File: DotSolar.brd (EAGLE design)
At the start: 25 x 35 mm, 24 parts, among them IC1 CAT24M010TS, IC2 SI1145, Q1 BSH203, U1 ISL29125

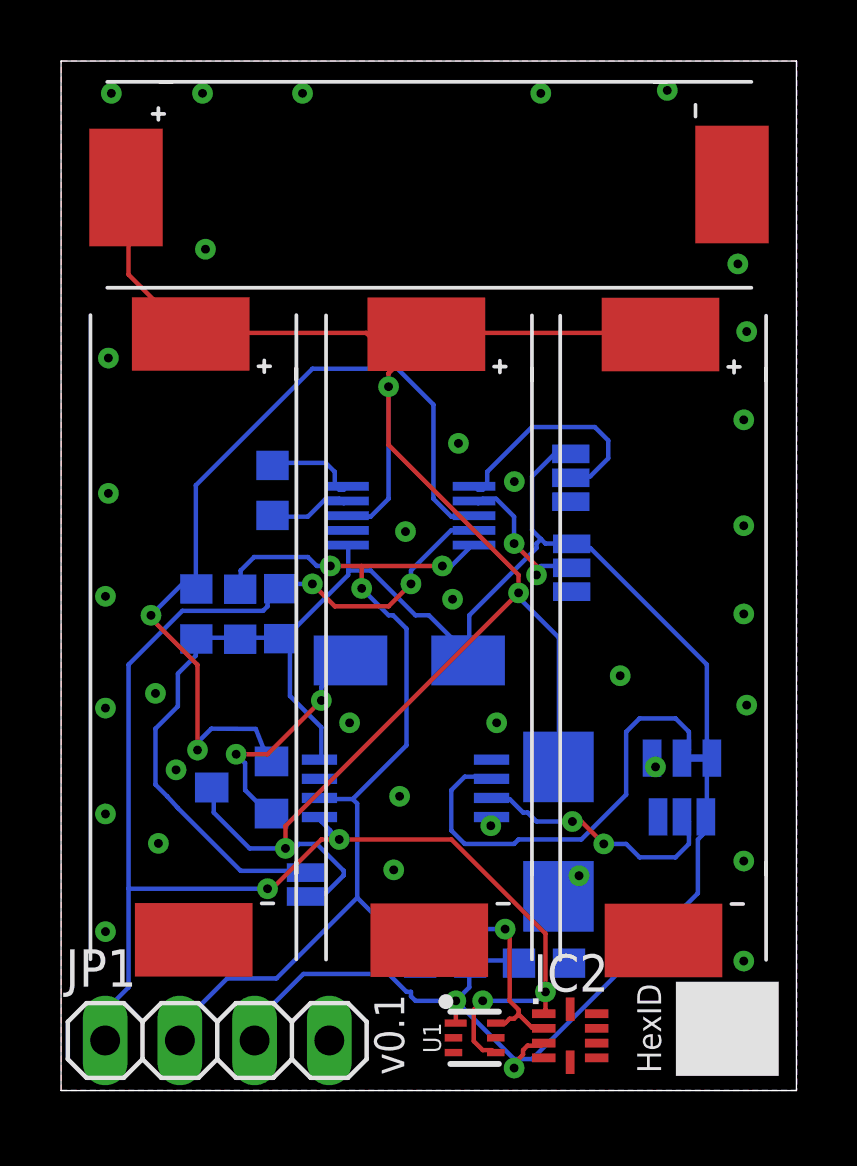
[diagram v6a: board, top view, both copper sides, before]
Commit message: Move zener
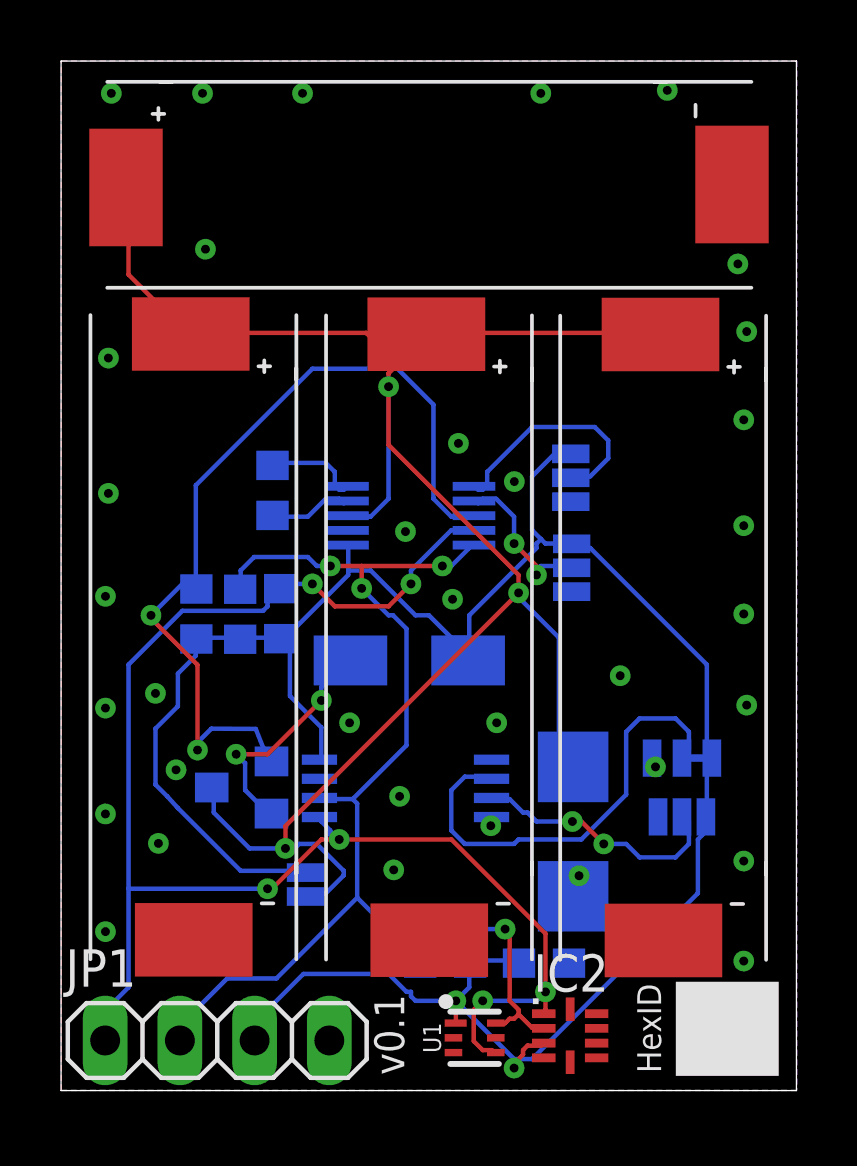
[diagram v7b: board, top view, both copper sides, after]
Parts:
- moved D3 0.50 mm to (17.4, 8.80)
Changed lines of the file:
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@@
 <layer number="22" name="bPlace" color="7" fill="1" visible="yes" active="yes"/>
 <layer number="23" name="tOrigins" color="15" fill="1" visible="no" active="yes"/>
-<layer number="24" name="bOrigins" color="15" fill="1" visible="no" active="yes"/>
+<layer number="24" name="bOrigins" color="15" fill="1" visible="yes" active="yes"/>
 <layer number="25" name="tNames" color="7" fill="1" visible="no" active="yes"/>
 <layer number="26" name="bNames" color="7" fill="1" visible="no" active="yes"/>
@@
 <element name="R2" library="rcl" package="R0603" value="4.7kΩ" x="7.44" y="16.21" rot="MR270"/>
 <element name="R3" library="rcl" package="R0603" value="4.7kΩ" x="6.08" y="16.19" rot="MR270"/>
-<element name="D3" library="diode" package="SMB" value="" x="16.9" y="8.8" rot="MR270"/>
+<element name="D3" library="diode" package="SMB" value="" x="17.4" y="8.8" rot="MR270"/>
 <element name="Q1" library="BSH203" package="SOT-23" value="BSH203" x="6.13" y="10.3" rot="MR270"/>
 <element name="U1" library="SparkFun-Sensors" package="ODFN-6" value="ISL29125" x="14.05" y="1.79">
@@
 <wire x1="11.1252" y1="21.9456" x2="15.5448" y2="17.526" width="0.1524" layer="1"/>
 <wire x1="11.1252" y1="23.9268" x2="11.1252" y2="21.9456" width="0.1524" layer="1"/>
-<wire x1="16.9164" y1="11.1252" x2="16.9" y2="11" width="0.1524" layer="16"/>
+<wire x1="16.9164" y1="11.1252" x2="17.4" y2="11" width="0.1524" layer="16"/>
 <wire x1="7.62" y1="8.9916" x2="7.62" y2="8.2296" width="0.1524" layer="1"/>
 <wire x1="15.5448" y1="16.9164" x2="7.62" y2="8.9916" width="0.1524" layer="1"/>

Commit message: Update tracks for production at Aisler
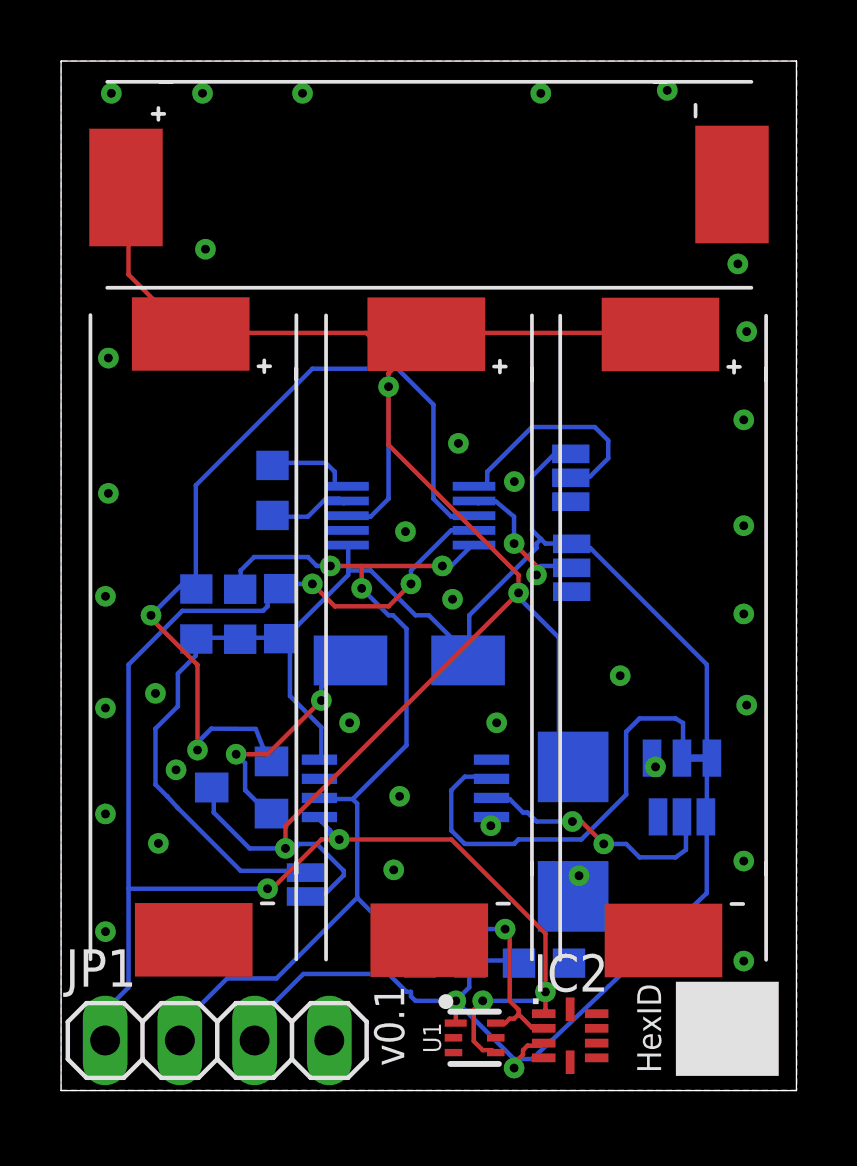
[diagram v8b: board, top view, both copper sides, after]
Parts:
- D1: value (none) -> B130-13-F
- D3: value (none) -> 3.3V
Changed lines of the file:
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@@
 <layer number="19" name="Unrouted" color="6" fill="1" visible="yes" active="yes"/>
 <layer number="20" name="Dimension" color="15" fill="1" visible="yes" active="yes"/>
-<layer number="21" name="tPlace" color="7" fill="1" visible="no" active="yes"/>
+<layer number="21" name="tPlace" color="7" fill="1" visible="yes" active="yes"/>
 <layer number="22" name="bPlace" color="7" fill="1" visible="yes" active="yes"/>
 <layer number="23" name="tOrigins" color="15" fill="1" visible="no" active="yes"/>
@@
 <layer number="39" name="tKeepout" color="4" fill="11" visible="no" active="yes"/>
 <layer number="40" name="bKeepout" color="1" fill="11" visible="no" active="yes"/>
-<layer number="41" name="tRestrict" color="4" fill="10" visible="no" active="yes"/>
-<layer number="42" name="bRestrict" color="1" fill="10" visible="no" active="yes"/>
+<layer number="41" name="tRestrict" color="4" fill="10" visible="yes" active="yes"/>
+<layer number="42" name="bRestrict" color="1" fill="10" visible="yes" active="yes"/>
 <layer number="43" name="vRestrict" color="2" fill="10" visible="no" active="yes"/>
 <layer number="44" name="Drills" color="7" fill="1" visible="no" active="yes"/>
@@
 <wire x1="-0.009" y1="34.9964" x2="-0.009" y2="-0.0036" width="0.01" layer="20"/>
 <text x="20.391" y="0.5964" size="0.8128" layer="21" rot="R90">HexID</text>
-<text x="10.641" y="3.2664" size="1.016" layer="21" rot="R270">v0.1</text>
+<text x="10.641" y="3.5664" size="1.016" layer="21" rot="R270">v0.1</text>
 <rectangle x1="20.891" y1="0.4964" x2="24.391" y2="3.6964" layer="21"/>
 <rectangle x1="11.0675" y1="22.4379" x2="11.2453" y2="22.4633" layer="22" rot="R180"/>
@@
 <rectangle x1="9.6663" y1="34.1183" x2="10.8347" y2="34.1437" layer="22" rot="R180"/>
 <text x="0.81" y="31.87" size="1.27" layer="22" rot="MR180">10.2017</text>
-<text x="5.02" y="14.55" size="0.8128" layer="22" rot="MR270">Alert</text>
-<text x="6.45" y="14.39" size="0.8128" layer="22" rot="MR270">SCL</text>
-<text x="7.88" y="14.55" size="0.8128" layer="22" rot="MR270">SDA</text>
-<rectangle x1="10.58" y1="0.32" x2="11.78" y2="3.23" layer="41"/>
-<rectangle x1="10.59" y1="0.31" x2="11.78" y2="3.23" layer="42"/>
+<text x="4.92" y="14.55" size="0.6096" layer="22" rot="MR270">Alert</text>
+<text x="6.35" y="14.49" size="0.6096" layer="22" rot="MR270">SCL</text>
+<text x="7.68" y="14.55" size="0.6096" layer="22" rot="MR270">SDA</text>
+<rectangle x1="10.58" y1="0.62" x2="11.78" y2="3.53" layer="41"/>
+<rectangle x1="10.59" y1="0.61" x2="11.78" y2="3.53" layer="42"/>
 <text x="18.69" y="17.29" size="0.8128" layer="22" rot="MR90">A0</text>
 <text x="18.65" y="20.44" size="0.8128" layer="22" rot="MR90">A1</text>
-<text x="0.5" y="7.5" size="0.8128" layer="22" rot="MR180">No Battery</text>
+<text x="0.9" y="7.5" size="0.6096" layer="22" rot="MR180">No Battery</text>
 <text x="0.2" y="-2.7" size="1.4224" layer="48">First solder the light sensors</text>
 <text x="20.9" y="22.1" size="0.6096" layer="22" rot="MR270">Current Sense</text>
@@
 <element name="R2" library="rcl" package="R0603" value="4.7kΩ" x="7.44" y="16.21" rot="MR270"/>
 <element name="R3" library="rcl" package="R0603" value="4.7kΩ" x="6.08" y="16.19" rot="MR270"/>
-<element name="D3" library="diode" package="SMB" value="" x="17.4" y="8.8" rot="MR270"/>
+<element name="D3" library="diode" package="SMB" value="3.3V" x="17.4" y="8.8" rot="MR270"/>
 <element name="Q1" library="BSH203" package="SOT-23" value="BSH203" x="6.13" y="10.3" rot="MR270"/>
 <element name="U1" library="SparkFun-Sensors" package="ODFN-6" value="ISL29125" x="14.05" y="1.79">
@@
 <element name="U$5" library="redan" package="VSSOP-10" value="INA226" x="11.88" y="19.54" rot="MR270"/>
 <element name="R4" library="rcl" package="R0603" value="4.7kΩ" x="4.59" y="16.2" rot="MR270"/>
-<element name="D1" library="PP_Passives" package="B130-13-F" value="" x="11.83" y="14.62" rot="MR0"/>
+<element name="D1" library="PP_Passives" package="B130-13-F" value="B130-13-F" x="11.83" y="14.62" rot="MR0"/>
 <element name="JP2" library="SparkFun-Jumpers" package="SMT-JUMPER_2_NO_SILK" value="NoBattery, only Capacitor" x="8.3" y="7" rot="MR90"/>
 <element name="U$6" library="IXYS_Solar_cells" package="KXOB22-01X8F_EXTENDED_PADS" value="KXOB22-01X8F_EXTENDED_PADS" x="4.8" y="15.12"/>
@@
 <wire x1="13.8684" y1="14.6304" x2="13.83" y2="14.62" width="0.1524" layer="16"/>
 <wire x1="16.002" y1="1.0668" x2="15.3924" y2="1.0668" width="0.1524" layer="16"/>
-<wire x1="21.6408" y1="6.7056" x2="16.002" y2="1.0668" width="0.1524" layer="16"/>
-<wire x1="21.6408" y1="8.5344" x2="21.6408" y2="6.7056" width="0.1524" layer="16"/>
-<wire x1="21.7932" y1="8.6868" x2="21.6408" y2="8.5344" width="0.1524" layer="16"/>
-<wire x1="21.7932" y1="9.2964" x2="21.7932" y2="8.6868" width="0.1524" layer="16"/>
+<wire x1="21.9408" y1="6.7056" x2="16.002" y2="1.0668" width="0.1524" layer="16"/>
+<wire x1="21.9408" y1="8.8344" x2="21.9408" y2="6.7056" width="0.1524" layer="16"/>
+<wire x1="21.7932" y1="8.8868" x2="21.9408" y2="8.8344" width="0.1524" layer="16"/>
+<wire x1="21.7932" y1="9.2964" x2="21.7932" y2="8.8868" width="0.1524" layer="16"/>
 <wire x1="15.3924" y1="1.0668" x2="15.3924" y2="0.762" width="0.1524" layer="16"/>
 <wire x1="21.7932" y1="9.2964" x2="21.9128" y2="9.3" width="0.1524" layer="16"/>
@@
 <wire x1="15.3924" y1="18.5928" x2="16.1544" y2="17.8308" width="0.1524" layer="1"/>
 <wire x1="15.3924" y1="19.5072" x2="15.3924" y2="18.5928" width="0.1524" layer="16"/>
-<wire x1="14.7828" y1="20.1168" x2="15.3924" y2="19.5072" width="0.1524" layer="16"/>
-<wire x1="14.3256" y1="20.1168" x2="14.7828" y2="20.1168" width="0.1524" layer="16"/>
-<wire x1="14.1732" y1="19.9644" x2="14.3256" y2="20.1168" width="0.1524" layer="16"/>
+<wire x1="14.7828" y1="20.0168" x2="15.3924" y2="19.5072" width="0.1524" layer="16"/>
+<wire x1="14.3256" y1="20.0168" x2="14.7828" y2="20.0168" width="0.1524" layer="16"/>
+<wire x1="14.1732" y1="19.9644" x2="14.3256" y2="20.0168" width="0.1524" layer="16"/>
 <wire x1="17.2212" y1="17.8308" x2="17.35" y2="17.77" width="0.1524" layer="16"/>
 <wire x1="14.1732" y1="19.9644" x2="14.03" y2="20.04" width="0.1524" layer="16"/>
@@
 <wire x1="14.478" y1="21.0312" x2="16.002" y2="22.5552" width="0.1524" layer="16"/>
 <wire x1="14.478" y1="20.574" x2="14.478" y2="21.0312" width="0.1524" layer="16"/>
-<wire x1="14.3256" y1="20.4216" x2="14.478" y2="20.574" width="0.1524" layer="16"/>
-<wire x1="14.1732" y1="20.4216" x2="14.3256" y2="20.4216" width="0.1524" layer="16"/>
+<wire x1="14.3256" y1="20.5216" x2="14.478" y2="20.574" width="0.1524" layer="16"/>
+<wire x1="14.1732" y1="20.5216" x2="14.3256" y2="20.5216" width="0.1524" layer="16"/>
 <wire x1="17.3736" y1="20.8788" x2="17.32" y2="20.83" width="0.1524" layer="16"/>
-<wire x1="14.1732" y1="20.4216" x2="14.03" y2="20.54" width="0.1524" layer="16"/>
+<wire x1="14.1732" y1="20.5216" x2="14.03" y2="20.54" width="0.1524" layer="16"/>
 </signal>
 <signal name="SDA">
@@
 <wire x1="9.2964" y1="21.0312" x2="8.9916" y2="21.336" width="0.1524" layer="16"/>
 <wire x1="9.2964" y1="20.574" x2="9.2964" y2="21.0312" width="0.1524" layer="16"/>
-<wire x1="9.4488" y1="20.4216" x2="9.2964" y2="20.574" width="0.1524" layer="16"/>
-<wire x1="9.6012" y1="20.4216" x2="9.4488" y2="20.4216" width="0.1524" layer="16"/>
+<wire x1="9.4488" y1="20.5216" x2="9.2964" y2="20.574" width="0.1524" layer="16"/>
+<wire x1="9.6012" y1="20.5216" x2="9.4488" y2="20.5216" width="0.1524" layer="16"/>
 <wire x1="7.3152" y1="21.336" x2="7.18" y2="21.25" width="0.1524" layer="16"/>
-<wire x1="9.6012" y1="20.4216" x2="9.73" y2="20.54" width="0.1524" layer="16"/>
+<wire x1="9.6012" y1="20.5216" x2="9.73" y2="20.54" width="0.1524" layer="16"/>
 </signal>
 <signal name="IN-">
@@
 <wire x1="19.6596" y1="12.6492" x2="19.2024" y2="12.192" width="0.1524" layer="16"/>
 <wire x1="20.8788" y1="12.6492" x2="19.6596" y2="12.6492" width="0.1524" layer="16"/>
-<wire x1="21.336" y1="12.192" x2="20.8788" y2="12.6492" width="0.1524" layer="16"/>
-<wire x1="21.336" y1="11.5824" x2="21.336" y2="12.192" width="0.1524" layer="16"/>
-<wire x1="21.1836" y1="11.43" x2="21.336" y2="11.5824" width="0.1524" layer="16"/>
+<wire x1="21.136" y1="12.492" x2="20.8788" y2="12.6492" width="0.1524" layer="16"/>
+<wire x1="21.136" y1="11.8824" x2="21.136" y2="12.492" width="0.1524" layer="16"/>
+<wire x1="21.1836" y1="11.43" x2="21.136" y2="11.8824" width="0.1524" layer="16"/>
 <wire x1="14.478" y1="10.668" x2="14.625" y2="10.595" width="0.1524" layer="16"/>
 <contactref element="JP3" pad="2"/>
@@
 <wire x1="19.6596" y1="7.9248" x2="19.2024" y2="8.382" width="0.1524" layer="16"/>
 <wire x1="20.8788" y1="7.9248" x2="19.6596" y2="7.9248" width="0.1524" layer="16"/>
-<wire x1="21.336" y1="8.382" x2="20.8788" y2="7.9248" width="0.1524" layer="16"/>
-<wire x1="21.336" y1="9.144" x2="21.336" y2="8.382" width="0.1524" layer="16"/>
-<wire x1="21.1836" y1="9.2964" x2="21.336" y2="9.144" width="0.1524" layer="16"/>
+<wire x1="21.236" y1="8.182" x2="20.8788" y2="7.9248" width="0.1524" layer="16"/>
+<wire x1="21.236" y1="8.944" x2="21.236" y2="8.182" width="0.1524" layer="16"/>
+<wire x1="21.1836" y1="9.2964" x2="21.236" y2="8.944" width="0.1524" layer="16"/>
 <wire x1="14.6304" y1="9.906" x2="14.625" y2="9.945" width="0.1524" layer="16"/>
 <wire x1="21.1836" y1="9.2964" x2="21.1" y2="9.3" width="0.1524" layer="16"/>
